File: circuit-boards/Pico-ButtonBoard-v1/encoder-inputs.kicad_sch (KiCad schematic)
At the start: 15 parts, among them J16 ENC PWR, J17 ENC0, J2 ENC1

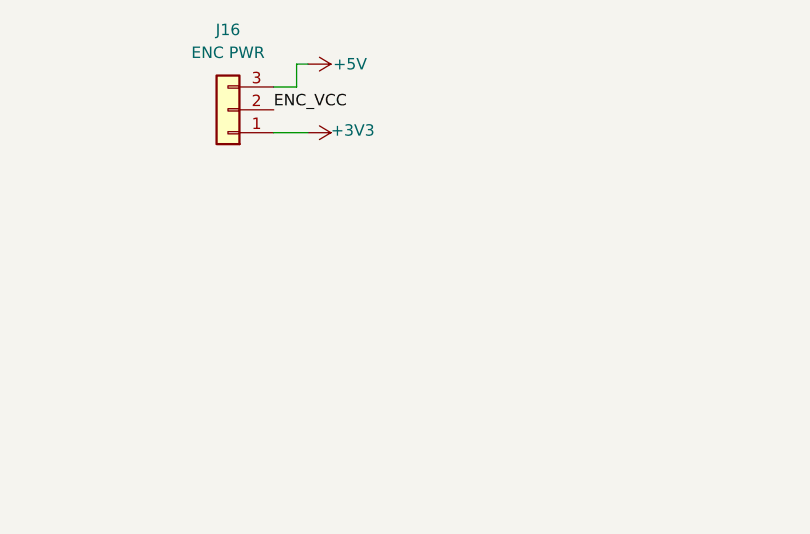
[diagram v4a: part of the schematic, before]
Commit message: Change diodes to schottky. Change 5V setpoint to 5.18V
Signed-off-by: Scott Berman <sgberman1@gmail.com>
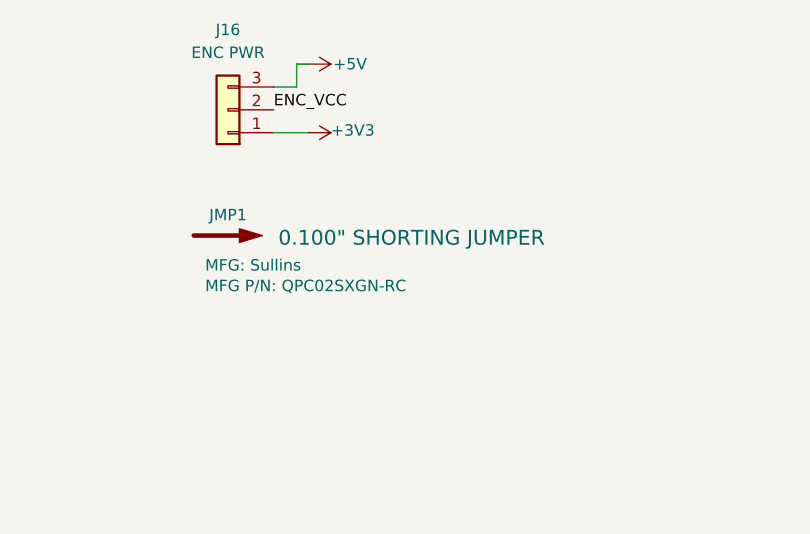
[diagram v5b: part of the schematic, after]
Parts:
- added JMP1: 0.100" SHORTING JUMPER, symbol Graphic:SYM_Arrow_Large
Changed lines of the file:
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@@
 	(title_block
 		(title "Pico Button Board")
-		(date "2025-12-30")
+		(date "2025-12-31")
 		(rev "1")
 	)
@@
 					(unit 1)
 				)
+			)
+		)
+	)
+	(symbol
+		(lib_id "Graphic:SYM_Arrow_Large")
+		(at 256.54 101.6 0)
+		(unit 1)
+		(exclude_from_sim no)
+		(in_bom yes)
+		(on_board no)
+		(dnp no)
+		(property "Reference" "JMP1"
+			(at 256.54 99.314 0)
+			(effects
+				(font
+					(size 1.27 1.27)
+				)
+			)
+		)
+		(property "Value" "0.100\" SHORTING JUMPER"
+			(at 262.128 101.854 0)
+			(effects
+				(font
+					(size 1.651 1.651)
+				)
+				(justify left)
+			)
+		)
+		(property "Footprint" ""
+			(at 256.54 101.6 0)
+			(effects
+				(font
+					(size 1.27 1.27)
+				)
+				(hide yes)
+			)
+		)
+		(property "Datasheet" ""
+			(at 256.54 101.6 0)
+			(effects
+				(font
+					(size 1.27 1.27)
+				)
+				(hide yes)
+			)
+		)
+		(property "Description" "2 (1 x 2) Position Shunt Connector Black Open Top 0.100\" (2.54mm) Gold"
+			(at 256.54 101.6 0)
+			(effects
+				(font
+					(size 1.27 1.27)
+				)
+				(hide yes)
+			)
+		)
+		(property "MFG" "Sullins"
+			(at 254 104.902 0)
+			(show_name yes)
+			(effects
+				(font
+					(size 1.27 1.27)
+				)
+				(justify left)
+			)
+		)
+		(property "MFG P/N" "QPC02SXGN-RC"
+			(at 254 107.188 0)
+			(show_name yes)
+			(effects
+				(font
+					(size 1.27 1.27)
+				)
+				(justify left)
+			)
+		)
+		(property "DIST" "Digikey"
+			(at 256.54 101.6 0)
+			(effects
+				(font
+					(size 1.27 1.27)
+				)
+				(hide yes)
+			)
+		)
+		(property "DIST P/N" "S9337-ND"
+			(at 256.54 101.6 0)
+			(effects
+				(font
+					(size 1.27 1.27)
+				)
+				(hide yes)
+			)
+		)
+		(instances
+			(project "Pico-ButtonBoard-v1"
+				(path "/644201a9-3a2f-4df3-9c93-2ae55394df4b/d0d9a62e-3d08-419e-af51-4493246764fe"
+					(reference "JMP1")
+					(unit 1)
+				)

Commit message: Added power indicator to button board
Signed-off-by: Scott Berman <sgberman1@gmail.com>
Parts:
- renumbered R63 to R68, R64 to R69, R65 to R70
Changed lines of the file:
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@@
 	(title_block
 		(title "Pico Button Board")
-		(date "2025-12-31")
+		(date "2026-01-20")
 		(rev "1")
 	)
@@
 		(on_board yes)
 		(dnp no)
-		(property "Reference" "R63"
+		(property "Reference" "R68"
 			(at 165.354 176.53 90)
 			(effects
@@
 			(project "Pico-ButtonBoard-v1"
 				(path "/644201a9-3a2f-4df3-9c93-2ae55394df4b/d0d9a62e-3d08-419e-af51-4493246764fe"
-					(reference "R63")
+					(reference "R68")
 					(unit 1)
 				)
@@
 		(on_board yes)
 		(dnp no)
-		(property "Reference" "R65"
+		(property "Reference" "R70"
 			(at 180.594 176.53 90)
 			(effects
@@
 			(project "Pico-ButtonBoard-v1"
 				(path "/644201a9-3a2f-4df3-9c93-2ae55394df4b/d0d9a62e-3d08-419e-af51-4493246764fe"
-					(reference "R65")
+					(reference "R70")
 					(unit 1)
 				)
@@
 		(on_board yes)
 		(dnp no)
-		(property "Reference" "R64"
+		(property "Reference" "R69"
 			(at 172.974 176.53 90)
 			(effects
@@
 			(project "Pico-ButtonBoard-v1"
 				(path "/644201a9-3a2f-4df3-9c93-2ae55394df4b/d0d9a62e-3d08-419e-af51-4493246764fe"
-					(reference "R64")
+					(reference "R69")
 					(unit 1)
 				)

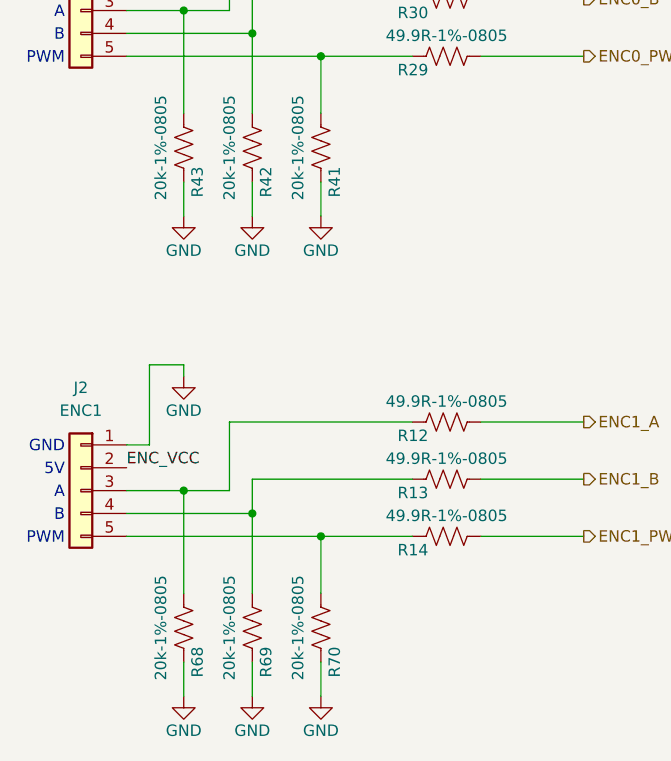
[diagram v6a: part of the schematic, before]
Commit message: Lower impedance of battery override input
Signed-off-by: Scott Berman <scott.berman@bluerivertech.com>
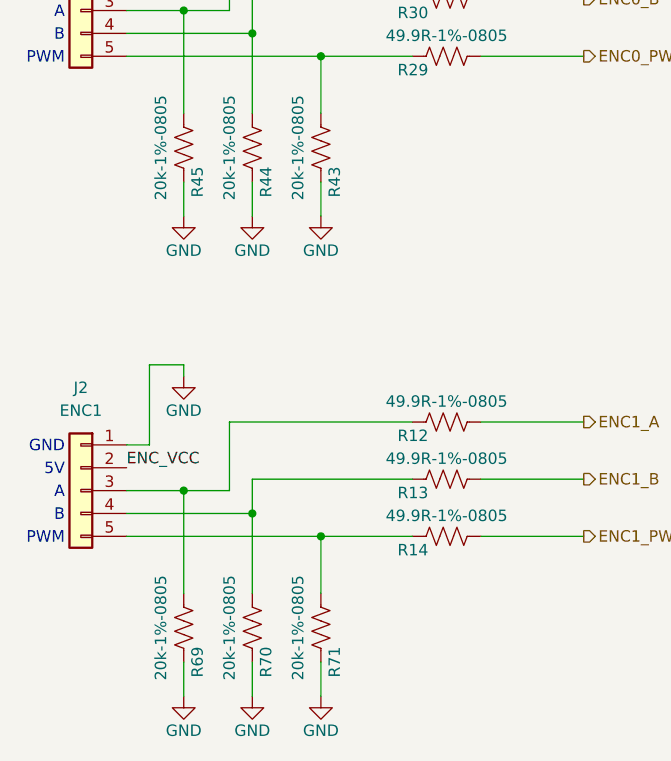
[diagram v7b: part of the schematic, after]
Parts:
- renumbered R41 to R43, R42 to R44, R43 to R45, R68 to R69, R69 to R70, R70 to R71
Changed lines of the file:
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@@
 	(title_block
 		(title "Pico Button Board")
-		(date "2026-01-20")
+		(date "2026-01-21")
 		(rev "1")
 	)
@@
 			)
 		)
+		(property "Sim.Pins" ""
+			(at 256.54 87.63 0)
+			(effects
+				(font
+					(size 1.27 1.27)
+				)
+				(hide yes)
+			)
+		)
 		(pin "2"
 		)
@@
 			)
 		)
+		(property "Sim.Pins" ""
+			(at 256.54 101.6 0)
+			(effects
+				(font
+					(size 1.27 1.27)
+				)
+				(hide yes)
+			)
+		)
 		(instances
 			(project "Pico-ButtonBoard-v1"
@@
 			)
 		)
+		(property "Sim.Pins" ""
+			(at 193.04 96.52 90)
+			(effects
+				(font
+					(size 1.27 1.27)
+				)
+				(hide yes)
+			)
+		)
 		(pin "1"
 		)
@@
 		(on_board yes)
 		(dnp no)
-		(property "Reference" "R68"
+		(property "Reference" "R69"
 			(at 165.354 176.53 90)
 			(effects
@@
 		(property "DIST P/N" "P20.0KCCT-ND"
 			(at 163.83 172.72 0)
+			(effects
+				(font
+					(size 1.27 1.27)
+				)
+				(hide yes)
+			)
+		)
+		(property "Sim.Pins" ""
+			(at 163.83 172.72 90)
 			(effects
 				(font
@@
 			(project "Pico-ButtonBoard-v1"
 				(path "/644201a9-3a2f-4df3-9c93-2ae55394df4b/d0d9a62e-3d08-419e-af51-4493246764fe"
-					(reference "R68")
+					(reference "R69")
 					(unit 1)
 				)
@@
 		(on_board yes)
 		(dnp no)
-		(property "Reference" "R70"
+		(property "Reference" "R71"
 			(at 180.594 176.53 90)
 			(effects
@@
 		(property "DIST P/N" "P20.0KCCT-ND"
 			(at 179.07 172.72 0)
+			(effects
+				(font
+					(size 1.27 1.27)
+				)
+				(hide yes)
+			)
+		)
+		(property "Sim.Pins" ""
+			(at 179.07 172.72 90)
 			(effects
 				(font
@@
 			(project "Pico-ButtonBoard-v1"
 				(path "/644201a9-3a2f-4df3-9c93-2ae55394df4b/d0d9a62e-3d08-419e-af51-4493246764fe"
-					(reference "R70")
+					(reference "R71")
 					(unit 1)
 				)
@@
 			)
 		)
+		(property "Sim.Pins" ""
+			(at 152.4 104.14 0)
+			(effects
+				(font
+					(size 1.27 1.27)
+				)
+				(hide yes)
+			)
+		)
 		(pin "4"
 		)
@@
 			)
 		)
+		(property "Sim.Pins" ""
+			(at 152.4 157.48 0)
+			(effects
+				(font
+					(size 1.27 1.27)
+				)
+				(hide yes)
+			)
+		)
 		(pin "4"
 		)
@@
 			)
 		)
+		(property "Sim.Pins" ""
+			(at 193.04 109.22 90)
+			(effects
+				(font
+					(size 1.27 1.27)
+				)
+				(hide yes)
+			)
+		)
 		(pin "1"
 		)
@@
 			)
 		)
+		(property "Sim.Pins" ""
+			(at 193.04 162.56 90)
+			(effects
+				(font
+					(size 1.27 1.27)
+				)
+				(hide yes)
+			)
+		)
 		(pin "1"
 		)
@@
 			)
 		)
+		(property "Sim.Pins" ""
+			(at 193.04 156.21 90)
+			(effects
+				(font
+					(size 1.27 1.27)
+				)
+				(hide yes)
+			)
+		)
 		(pin "1"
 		)
@@
 			)
 		)
+		(property "Sim.Pins" ""
+			(at 193.04 102.87 90)
+			(effects
+				(font
+					(size 1.27 1.27)
+				)
+				(hide yes)
+			)
+		)
 		(pin "1"
 		)
@@
 		(on_board yes)
 		(dnp no)
-		(property "Reference" "R69"
+		(property "Reference" "R70"
 			(at 172.974 176.53 90)
 			(effects
@@
 		(property "DIST P/N" "P20.0KCCT-ND"
 			(at 171.45 172.72 0)
+			(effects
+				(font
+					(size 1.27 1.27)
+				)
+				(hide yes)
+			)
+		)
+		(property "Sim.Pins" ""
+			(at 171.45 172.72 90)
 			(effects
 				(font
@@
 			(project "Pico-ButtonBoard-v1"
 				(path "/644201a9-3a2f-4df3-9c93-2ae55394df4b/d0d9a62e-3d08-419e-af51-4493246764fe"
-					(reference "R69")
+					(reference "R70")
 					(unit 1)
 				)
@@
 			)
 		)
+		(property "Sim.Pins" ""
+			(at 193.04 149.86 90)
+			(effects
+				(font
+					(size 1.27 1.27)
+				)
+				(hide yes)
+			)
+		)
 		(pin "1"
 		)
@@
 		(on_board yes)
 		(dnp no)
-		(property "Reference" "R41"
+		(property "Reference" "R43"
 			(at 180.594 123.19 90)
 			(effects
@@
 			)
 		)
-		(pin "1"
-		)
-		(pin "2"
-		)
-		(instances
-			(project "Pico-ButtonBoard-v1"
-				(path "/644201a9-3a2f-4df3-9c93-2ae55394df4b/d0d9a62e-3d08-419e-af51-4493246764fe"
-					(reference "R41")
-					(unit 1)
-				)
-			)
-		)
-	)
-	(symbol
-		(lib_id "Device:R_US")
-		(at 163.83 119.38 180)
-		(unit 1)
-		(exclude_from_sim no)
-		(in_bom yes)
-		(on_board yes)
-		(dnp no)
-		(property "Reference" "R43"
-			(at 165.354 123.19 90)
-			(effects
-				(font
-					(size 1.27 1.27)
-				)
-			)
-		)
-		(property "Value" "20k-1%-0805"
-			(at 161.29 119.38 90)
-			(effects
-				(font
-					(size 1.27 1.27)
-				)
-			)
-		)
-		(property "Footprint" "Resistor_SMD:R_0805_2012Metric_Pad1.20x1.40mm_HandSolder"
-			(at 162.814 119.126 90)
-			(effects
-				(font
-					(size 1.27 1.27)
-				)
-				(hide yes)
-			)
-		)
-		(property "Datasheet" "~"
-			(at 163.83 119.38 0)
-			(effects
-				(font
-					(size 1.27 1.27)
-				)
-				(hide yes)
-			)
-		)
-		(property "Description" "Resistor, US symbol"
-			(at 163.83 119.38 0)
-			(effects
-				(font
-					(size 1.27 1.27)
-				)
-				(hide yes)
-			)
-		)
-		(property "MFG" "Panasonic"
-			(at 163.83 119.38 0)
-			(effects
-				(font
-					(size 1.27 1.27)
-				)
-				(hide yes)
-			)
-		)
-		(property "MFG P/N" "ERJ-6ENF2002V"
-			(at 163.83 119.38 0)
-			(effects
-				(font
-					(size 1.27 1.27)
-				)
-				(hide yes)
-			)
-		)
-		(property "DIST" "Digikey"
-			(at 163.83 119.38 0)
-			(effects
-				(font
-					(size 1.27 1.27)
-				)
-				(hide yes)
-			)
-		)
-		(property "DIST P/N" "P20.0KCCT-ND"
-			(at 163.83 119.38 0)
+		(property "Sim.Pins" ""
+			(at 179.07 119.38 90)
 			(effects
 				(font
@@
 	)
 	(symbol
+		(lib_id "Device:R_US")
+		(at 163.83 119.38 180)
+		(unit 1)
+		(exclude_from_sim no)
+		(in_bom yes)
+		(on_board yes)
+		(dnp no)
+		(property "Reference" "R45"
+			(at 165.354 123.19 90)
+			(effects
+				(font
+					(size 1.27 1.27)
+				)
+			)
+		)
+		(property "Value" "20k-1%-0805"
+			(at 161.29 119.38 90)
+			(effects
+				(font
+					(size 1.27 1.27)
+				)
+			)
+		)
+		(property "Footprint" "Resistor_SMD:R_0805_2012Metric_Pad1.20x1.40mm_HandSolder"
+			(at 162.814 119.126 90)
+			(effects
+				(font
+					(size 1.27 1.27)
+				)
+				(hide yes)
+			)
+		)
+		(property "Datasheet" "~"
+			(at 163.83 119.38 0)
+			(effects
+				(font
+					(size 1.27 1.27)
+				)
+				(hide yes)
+			)
+		)
+		(property "Description" "Resistor, US symbol"
+			(at 163.83 119.38 0)
+			(effects
+				(font
+					(size 1.27 1.27)
+				)
+				(hide yes)
+			)
+		)
+		(property "MFG" "Panasonic"
+			(at 163.83 119.38 0)
+			(effects
+				(font
+					(size 1.27 1.27)
+				)
+				(hide yes)
+			)
+		)
+		(property "MFG P/N" "ERJ-6ENF2002V"
+			(at 163.83 119.38 0)
+			(effects
+				(font
+					(size 1.27 1.27)
+				)
+				(hide yes)
+			)
+		)
+		(property "DIST" "Digikey"
+			(at 163.83 119.38 0)
+			(effects
+				(font
+					(size 1.27 1.27)
+				)
+				(hide yes)
+			)
+		)
+		(property "DIST P/N" "P20.0KCCT-ND"
+			(at 163.83 119.38 0)
+			(effects
+				(font
+					(size 1.27 1.27)
+				)
+				(hide yes)
+			)
+		)
+		(property "Sim.Pins" ""
+			(at 163.83 119.38 90)
+			(effects
+				(font
+					(size 1.27 1.27)
+				)
+				(hide yes)
+			)
+		)
+		(pin "1"
+		)
+		(pin "2"
+		)
+		(instances
+			(project "Pico-ButtonBoard-v1"
+				(path "/644201a9-3a2f-4df3-9c93-2ae55394df4b/d0d9a62e-3d08-419e-af51-4493246764fe"
+					(reference "R45")
+					(unit 1)
+				)
+			)
+		)
+	)
+	(symbol
 		(lib_id "power:GND")
 		(at 171.45 127 0)
@@
 		(on_board yes)
 		(dnp no)
-		(property "Reference" "R42"
+		(property "Reference" "R44"
 			(at 172.974 123.19 90)
 			(effects
@@
 		(property "DIST P/N" "P20.0KCCT-ND"
 			(at 171.45 119.38 0)
+			(effects
+				(font
+					(size 1.27 1.27)
+				)
+				(hide yes)
+			)
+		)
+		(property "Sim.Pins" ""
+			(at 171.45 119.38 90)
 			(effects
 				(font
@@
 			(project "Pico-ButtonBoard-v1"
 				(path "/644201a9-3a2f-4df3-9c93-2ae55394df4b/d0d9a62e-3d08-419e-af51-4493246764fe"
-					(reference "R42")
+					(reference "R44")
 					(unit 1)
 				)
